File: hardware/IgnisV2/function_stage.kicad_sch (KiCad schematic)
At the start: 27 parts, among them J4 Conn_01x01_Pin, SW1 SW-18030, U4 74LVC1G17, U5 ATtiny212-SS

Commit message: 🏭 Finalize IgnisV2 PCB design and prepare for JLCPCB production
- Polished hierarchical schematics with clean signal routing
- Completed full PCB layout with optimized component placement
- Refined component selection for optimal JLCPCB compatibility
- Generated production files (Gerbers, drill, BOM, pick&place) for fabrication
- Exported 3D model snapshot for documentation and review
- Added 74LVC1G17 datasheet for package selection reference
- Selected TSSOP-5 package over SOT1202 for PCBA compatibility
- Configured for advanced PCBA service due to WS2812B backing requirements
- Updated design rules and gitignore for production workflow
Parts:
- added H1, H2, H3: ToolingHole, MountingHole:ToolingHole_1.152mm, symbol Mechanical:MountingHole
- added J5: VSYS, TestPoint:TestPoint_THTPad_D1.5mm_Drill0.7mm, symbol Connector:Conn_01x01_Pin
- added J6: GND, TestPoint:TestPoint_THTPad_D1.5mm_Drill0.7mm, symbol Connector:Conn_01x01_Pin
- J4: value Conn_01x01_Pin -> UPDI; footprint Connector_Wire:SolderWire-0.5sqmm_1x01_D0.9mm_OD2.1mm -> TestPoint:TestPoint_THTPad_D1.5mm_Drill0.7mm
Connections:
- net GND: now also J6.1 (Pin_1)
- net LED_DIN: now also TP12.1
- net at D2.4 (DIN), R16.2: no longer TP12.1
- net ~{STBY} renamed ~{PGOOD}
- new net VSYS: J5.1 (Pin_1)
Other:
- moved on the sheet: J4, TP12

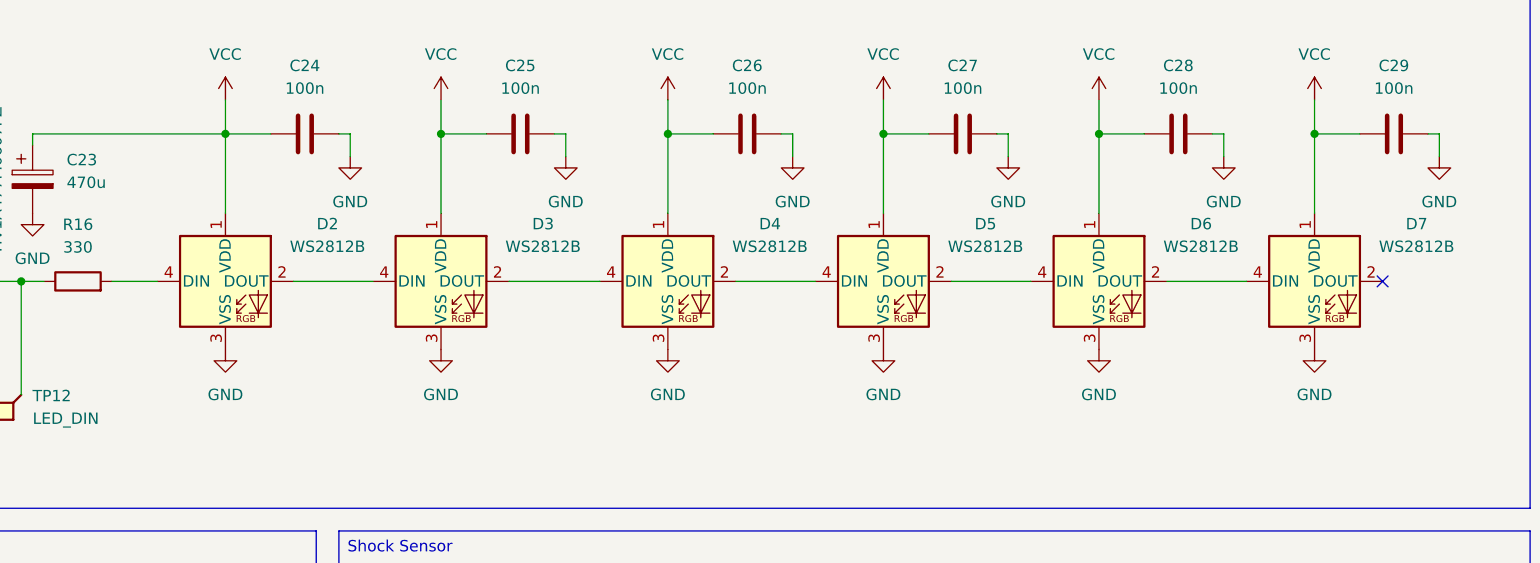
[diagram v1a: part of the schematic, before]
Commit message: 🚨 Fix critical PCB issues caught during JLCPCB review
- Fixed undersized vias (<0.3mm) in component footprints to avoid extra costs
- Corrected WS2812B symbol pinout mismatch between standard and 2020 package
- Updated WS2812B-2020 wiring to match proper pin assignments
- Regenerated production files with corrected drill sizes and routing

**Critical catch: WS2812B standard vs 2020 package have different pinouts!**

Production halted and corrected before fabrication.
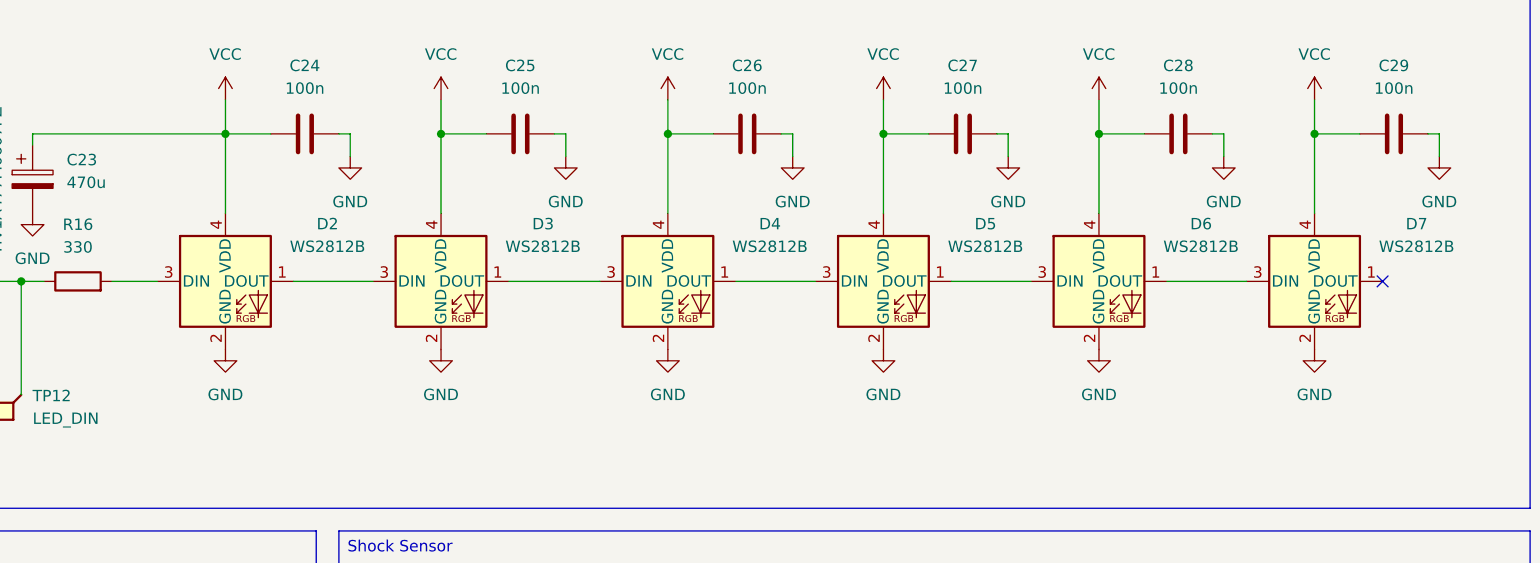
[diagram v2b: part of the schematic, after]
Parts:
- D2, D3, D4, D5, D6, D7: symbol LED:WS2812B -> Ignis:WS2812B
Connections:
- net GND: now also D2.2 (GND), D3.2 (GND), D4.2 (GND), D5.2 (GND), D6.2 (GND), D7.2 (GND); no longer D2.3 (VSS), D3.3 (VSS), D4.3 (VSS), D5.3 (VSS), D6.3 (VSS), D7.3 (VSS)
- net VCC: now also D2.4 (VDD), D3.4 (VDD), D4.4 (VDD), D5.4 (VDD), D6.4 (VDD), D7.4 (VDD); no longer D2.1 (VDD), D3.1 (VDD), D4.1 (VDD), D5.1 (VDD), D6.1 (VDD), D7.1 (VDD)
- net at R16.2: now also D2.3 (DIN); no longer D2.4 (DIN)
- new net: D3.1 (DOUT), D4.3 (DIN)
- new net: D2.1 (DOUT), D3.3 (DIN)
- new net: D6.1 (DOUT), D7.3 (DIN)
- new net: D5.1 (DOUT), D6.3 (DIN)
- new net: D4.1 (DOUT), D5.3 (DIN)
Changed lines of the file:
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@@
 	)
 	(symbol
-		(lib_id "LED:WS2812B")
+		(lib_id "Ignis:WS2812B")
 		(at 160.02 48.26 0)
 		(unit 1)
@@
 	)
 	(symbol
-		(lib_id "LED:WS2812B")
+		(lib_id "Ignis:WS2812B")
 		(at 257.81 48.26 0)
 		(unit 1)
@@
 	)
 	(symbol
-		(lib_id "LED:WS2812B")
+		(lib_id "Ignis:WS2812B")
 		(at 233.68 48.26 0)
 		(unit 1)
@@
 	)
 	(symbol
-		(lib_id "LED:WS2812B")
+		(lib_id "Ignis:WS2812B")
 		(at 209.55 48.26 0)
 		(unit 1)
@@
 	)
 	(symbol
-		(lib_id "LED:WS2812B")
+		(lib_id "Ignis:WS2812B")
 		(at 185.42 48.26 0)
 		(unit 1)
@@
 	)
 	(symbol
-		(lib_id "LED:WS2812B")
+		(lib_id "Ignis:WS2812B")
 		(at 135.89 48.26 0)
 		(unit 1)

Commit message: 🎨 Complete logo cleanup and rebranding with new typography
- Changed official logo font from Museo Rounded to "Dongle" Bold
- Reorganized logo assets with consistent naming convention
- Added Makefile for automated PNG export in multiple variants and sizes
- Updated KiCAD worksheets for both IgnisV1 and IgnisV2 PCBs with new branding
- Removed obsolete logo files and consolidated SVG sources
- Exported updated schematic PDFs with refreshed corporate identity
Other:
- title: (none) -> Ignis
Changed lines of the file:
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@@
 	(generator_version "9.0")
 	(paper "A4")
+	(title_block
+		(title "Ignis")
+		(date "2025-08-26")
+		(rev "v2.2")
+	)
 	(text "Simplified on-board electronics:\nUPDI circuitry is on programmer board"
 		(exclude_from_sim no)
